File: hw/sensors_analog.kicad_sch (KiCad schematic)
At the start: 47 parts, among them U1 OPAMP_GENERIC, U2 OPAMP_GENERIC, U3 OPAMP_GENERIC, U4 OPAMP_GENERIC, U5 OPAMP_GENERIC

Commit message: Wire the root sheet: the project has a netlist for the first time
Ten sheets each passed their own netlist and the project had none. The
root sheet's ten sheet symbols carried NO hierarchical pins, so a net
name appearing on two sheets was two nets and nothing compared them --
the cross-sheet audit in the last commit was a name comparison, not a
connectivity check.

Each symbol now carries one pin per net its child exports, read OUT of
the child rather than declared in a second list that could drift: 162
pins across the ten, each with a stub and a label. Two labels with the
same name are one net, which is how 162 pins connect without routing
162 wires across a page nobody could read.

Exporting it found the other half of the same problem immediately.
kicad-cli reported annotation errors: every sheet generator allocated
R1, C1, U1 from its own counter, so ten sheets had ten parts called R1.
schlib.REF_BASE gives each sheet its own hundred -- KiCad's own
sheet-number x 100 convention, applied at generation time instead of by
a hand pass in Eeschema. 196 components, no duplicate reference.

hw/check_netlist.py is the gate, and the counterpart to sim/run_sim.py:
that one guards the component values, this one guards the connectivity.
Same rule -- an exemption is not a pass. Every single-pin net is listed
with its reason, and a net that STOPS being single-pin fails the check
until it is removed from the list. An open item that quietly closes is
as much a drift as one that quietly opens.

  196 components, every reference unique
  113 named nets carrying two or more pins
   18 named nets reaching one pin, each a recorded open item
      GND 134 pins, 3V3_MCU 27, VBAT_PROT 12 -- all spanning the project

The root sheet carries those eighteen on the page itself, grouped by
what they wait on, so a reader does not have to run a script to find
which ends are loose.

Full set plots to docs/pdf/ECU-Schematics.pdf, 11 pages.

Two rendering bugs fixed: sheet pin names and their stu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
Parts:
- removed C1, C2, C3, C4, C5, C6, C7, C8: 22nF, symbol Device:C
- removed D1, D2, D3, D4, D5, D6, D7, D8: 3.3V, symbol Device:D_Zener
- removed R1, R3: 120k, symbol Device:R
- removed R10, R12, R14, R16, R18, R20, R22, R24, R26, R6, R8: 16k, symbol Device:R
- removed R11, R13, R15, R17, R19, R21, R23, R25, R7, R9: 26k, symbol Device:R
- removed R2, R4, R5: 10k, symbol Device:R
- removed U1, U2, U3, U4, U5: OPAMP_GENERIC, symbol ecu25kva:OPAMP_GENERIC
- added C601, C602, C603, C604, C605, C606, C607, C608: 22nF, symbol Device:C
- added D601, D602, D603, D604, D605, D606, D607, D608: 3.3V, symbol Device:D_Zener
- added R601, R603: 120k, symbol Device:R
- added R602, R604, R605: 10k, symbol Device:R
- added R606, R608, R610, R612, R614, R616, R618, R620, R622, R624, R626: 16k, symbol Device:R
- added R607, R609, R611, R613, R615, R617, R619, R621, R623, R625: 26k, symbol Device:R
- added U601, U602, U603, U604, U605: OPAMP_GENERIC, symbol ecu25kva:OPAMP_GENERIC
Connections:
- net 5V_MAIN: now also U601.5 (V+), U602.5 (V+), U603.5 (V+), U604.5 (V+), U605.5 (V+)
- net BOOST_P: now also C604.1, D604.1 (K), R610.2, U601.1 (OUT)
- net BOOST_P_IN: now also R607.1
- net BOOST_T: now also C608.1, D608.1 (K), R626.2, U605.1 (OUT)
- net BOOST_T_IN: now also R623.1
- net COOLANT_T: now also C605.1, D605.1 (K), R614.2, U602.1 (OUT)
- net COOLANT_T_IN: now also R611.1
- net EGR_POS: now also C606.1, D606.1 (K), R618.2, U603.1 (OUT)
- net EGR_POS_IN: now also R615.1
- net GND: now also C601.2, C602.2, C603.2, C604.2, C605.2, C606.2, C607.2, C608.2, D601.2 (A), D602.2 (A), D603.2 (A), D604.2 (A), D605.2 (A), D606.2 (A), D607.2 (A), D608.2 (A), R602.2, R604.2, R606.2, R608.2, R612.2, R616.2, R620.2, R624.2, U601.4 (V-), U602.4 (V-), U603.4 (V-), U604.4 (V-), U605.4 (V-)
- net OIL_P: now also C607.1, D607.1 (K), R622.2, U604.1 (OUT)
- net OIL_P_IN: now also R619.1
- net RAIL_P: now also C603.1, D603.1 (K), R605.2, R606.1
- net RAIL_P_IN: now also R605.1
- net SGND_34: now also R609.1, R613.1, R625.1
- net SGND_36: now also R617.1, R621.1
- net V_BAT_1R: now also R601.1
- net V_BAT_1R_SNS: now also C601.1, D601.1 (K), R601.2, R602.1
- net V_BAT_2R: now also R603.1
- net V_BAT_2R_SNS: now also C602.1, D602.1 (K), R603.2, R604.1
- new net: R621.2, R622.1, U604.2 (IN-)
- new net: R619.2, R620.1, U604.3 (IN+)
- new net: R623.2, R624.1, U605.3 (IN+)
- new net: R615.2, R616.1, U603.3 (IN+)
- new net: R613.2, R614.1, U602.2 (IN-)
- new net: R609.2, R610.1, U601.2 (IN-)
- new net: R607.2, R608.1, U601.3 (IN+)
- new net: R617.2, R618.1, U603.2 (IN-)
- new net: R625.2, R626.1, U605.2 (IN-)
- new net: R611.2, R612.1, U602.3 (IN+)

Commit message: Check the project netlist, and fix the three things it caught
hw/check_netlist.py grew the two checks that found them, so neither can
come back quietly. It is the counterpart to sim/run_sim.py: that one
guards the component values, this one guards the connectivity.

5V_MAIN WAS FOUR NETS. The buck's 5 V output is a board rail -- both CAN
transceivers' VCC, the five difference amplifiers and the discrete
inputs' pull-ups run off it -- and it was a LOCAL label on every one of
those sheets. A local label stops at its sheet's edge, so three of the
four copies had no regulator on them. Each sheet's own netlist was
correct, which is exactly why ten clean per-sheet netlists never found
it. rails now exports it as a hierarchical label.

3V3_MCU WAS THREE. Same mechanism on can (both transceivers' VIO) and
speed_inputs, where the comparator's supply, both upper clamp diodes and
the bias divider sat on a five-pin net with no rail attached.

New check: any sheet-local net whose name shadows a project-wide net
name fails. That is the exact shape of both defects.

FIVE SUPPLY PINS HAD NO DECOUPLING CAPACITOR. The difference amplifiers
on sensors_analog were the only undecoupled supply pins on the board. No
simulation block was ever going to say so -- sensor_differential.cir
models an ideal amplifier with no supply pin at all. 100 nF each, at the
pin.

New check: walk every power_in pin in the project netlist and ask
whether a capacitor sits on the same net. 22 supply pins, all covered.
One documented exemption, the LM5164's BST pin, whose bootstrap
capacitor IS the net.

Gate now: 201 components with unique references, 108 named nets carrying
two or more pins, 18 reaching one and each a recorded open item, GND 139
pins, 3V3_MCU 36, 5V_MAIN 28, VBAT_PROT 12.

Schematic set re-plotted: docs/pdf/ECU-Schematics.pdf, 11 pages.
Suite still 24/24.

Co-Authored-By: Claude Opus 5 <noreply@anthropic.com>
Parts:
- added C609, C611, C613: 22nF, symbol Device:C
- added C610, C612: 100nF, symbol Device:C
- C604, C606, C608: value 22nF -> 100nF; Note With the 16k below it, 0.35 ms -- fast against the engine a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 -> One per amplifier is the conservative count. Five channels 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; Source sensor_ratiometric.cir C1 -> hw/check_netlist.py decoupling audit
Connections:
- net 5V_MAIN: now also C604.1, C606.1, C608.1, C610.1, C612.1
- net BOOST_P: now also C605.1; no longer C604.1
- net BOOST_T: now also C613.1; no longer C608.1
- net COOLANT_T: now also C607.1; no longer C605.1
- net EGR_POS: now also C609.1; no longer C606.1
- net GND: now also C609.2, C610.2, C611.2, C612.2, C613.2
- net OIL_P: now also C611.1; no longer C607.1

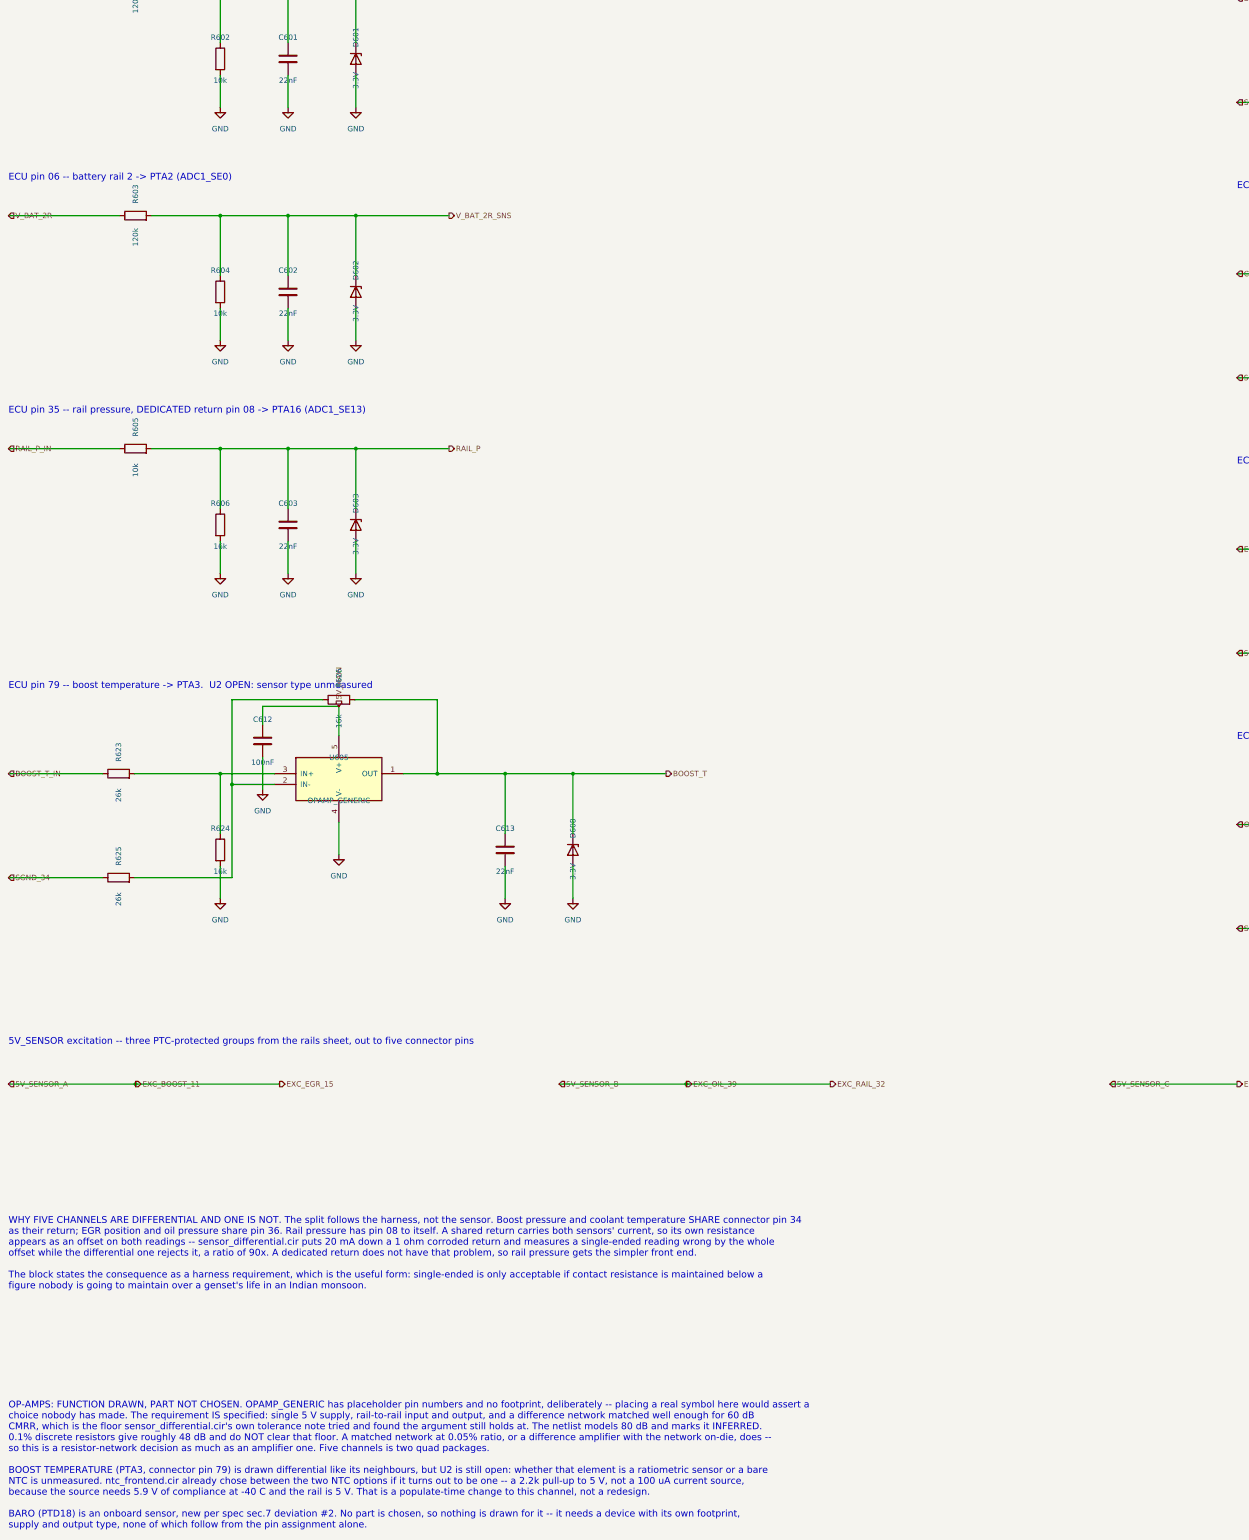
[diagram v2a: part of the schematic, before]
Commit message: Draw the onboard barometric sensor; one open end left, and it needs the machine
Spec sec.7 deviation 2 adds the baro on purpose: on-PCB behind a vented
port, costs nothing in harness terms, improves fuelling correction.

NXP MPXHZ6115A6T1, from the retrieved MPXA6115A series data sheet
(Rev. 7.3): 15-115 kPa, VOUT = VS(0.009P - 0.095), pins 1 DNC / 2 VS /
3 GND / 4 VOUT / 5-8 DNC, case 98ARH99066A -- a footprint KiCad ships,
whose pads 1-8 were checked against the datasheet's pin table.

Supplied from 5V_MAIN, which SENSOR_5V_MON already measures, so the
reading is ratiometric-correctable with no new channel. Through the same
10k/16k divider the sheet's other 5 V channels use: 2.51 V at sea level,
1.92 V at 2000 m, and no zener -- every other channel on that sheet
arrives from the harness and this one never leaves the board.

NOT STATED AEC-Q100 in the retrieved datasheet, and that is recorded
rather than assumed away. Infineon's KP236 is listed automotive-qualified
(40-115 kPa) and would be the choice, but its datasheet did not resolve
by any route -- Mouser timed out twice, Infineon's own host redirected --
and it is a footprint change, not a drop-in.

Open ends 2 -> 1. TRIP_LOOP remains, and no part closes it: it is a new
signal, not on the OEM diagram, and needs a connector pin AND a harness
wire -- field-brief task 5.2.

ONE DISAGREEMENT FOUND ON THE WAY, recorded in status.md for a decision
rather than fixed: spec sec.7 deviation 1 says the ECU uses functionally
split sealed connectors with an adapter harness to the OEM loom, and
hw/connector.kicad_sch draws the OEM 94-way on the board. The electrical
content is identical either way; the physical part and the adapter are a
scope decision.

24/24 blocks, 24/24 netlist checks, 44 supply pins decoupled.

Co-Authored-By: Claude Opus 5 <noreply@anthropic.com>
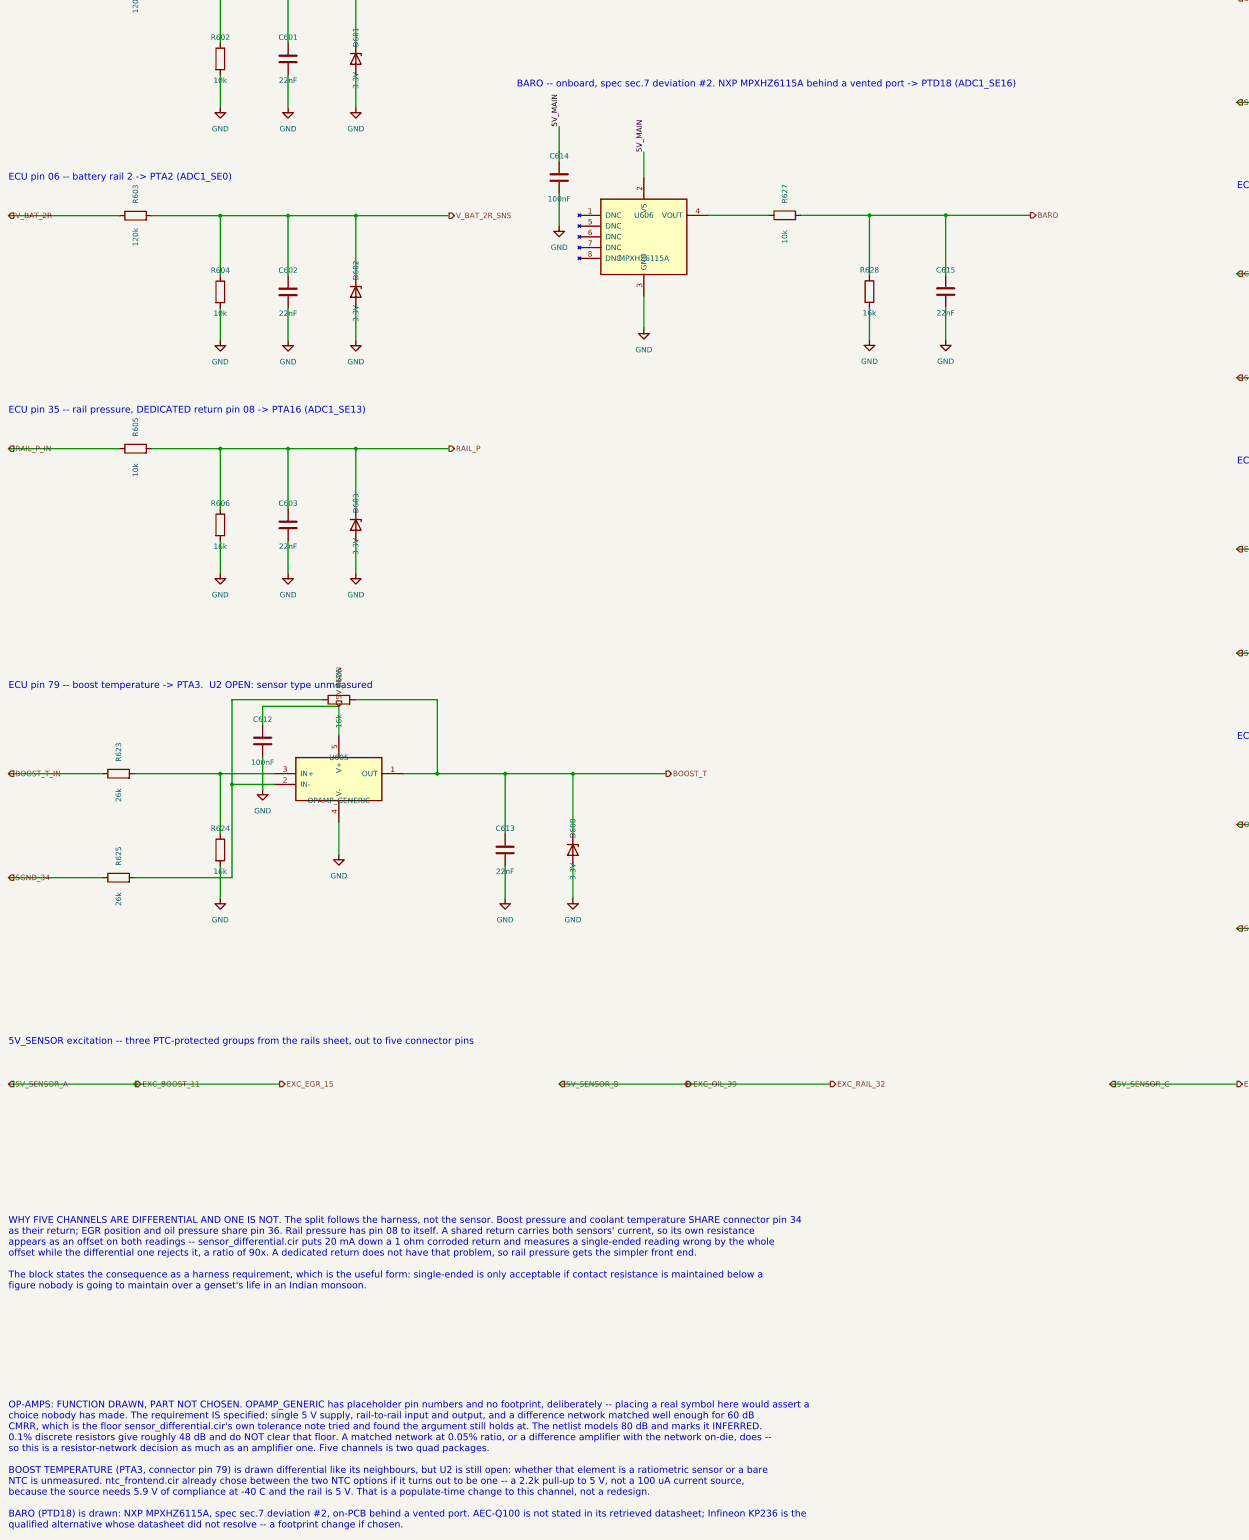
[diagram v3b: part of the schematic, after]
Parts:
- added C614: 100nF, symbol Device:C
- added C615: 22nF, symbol Device:C
- added R627: 10k, symbol Device:R
- added R628: 16k, symbol Device:R
- added U606: MPXHZ6115A, Sensor_Pressure:Freescale_98ARH99066A, symbol ecu25kva:MPXHZ6115A
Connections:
- net 5V_MAIN: now also C614.1, U606.2 (VS)
- net GND: now also C614.2, C615.2, R628.2, U606.3 (GND)
- new net: R627.1, U606.4 (VOUT)
- new net BARO: C615.1, R627.2, R628.1
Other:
- note added: "BARO -- onboard, spec sec.7 deviation #2. NXP MPXHZ6115A behind a vented port -> PTD18 (ADC1_SE16)"
